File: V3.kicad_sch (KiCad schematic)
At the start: 33 parts, among them J5 MicroMatch, J6 MicroMatch, U1 TL072, U2 TL072, U3 TL072

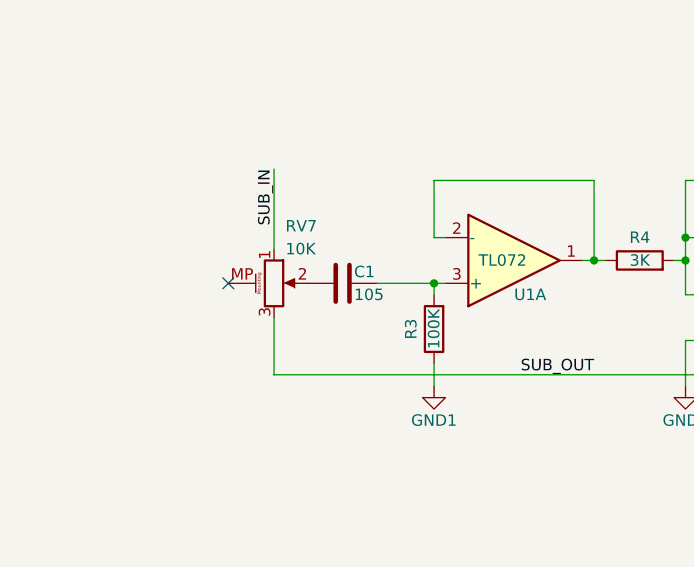
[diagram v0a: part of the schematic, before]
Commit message: Oops, all of the single gang pots were backwards - fixed.
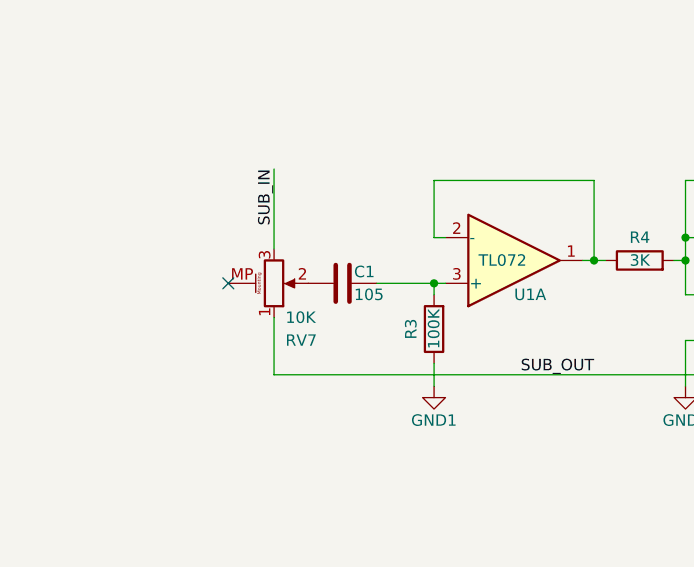
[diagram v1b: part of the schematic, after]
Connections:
- net SUB_IN: now also RV7.3; no longer RV7.1
- net SUB_OUT: now also RV7.1; no longer RV7.3
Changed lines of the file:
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@@
 		(lib_id "Device:R_Potentiometer_MountingPin")
 		(at 63.5 101.6 0)
+		(mirror x)
 		(unit 1)
 		(exclude_from_sim no)
@@
 		(dnp no)
 		(property "Reference" "RV7"
-			(at 64.77 95.25 0)
+			(at 64.77 107.95 0)
 			(effects
 				(font
@@
 		)
 		(property "Value" "10K"
-			(at 64.77 97.79 0)
+			(at 64.77 105.41 0)
 			(effects
 				(font

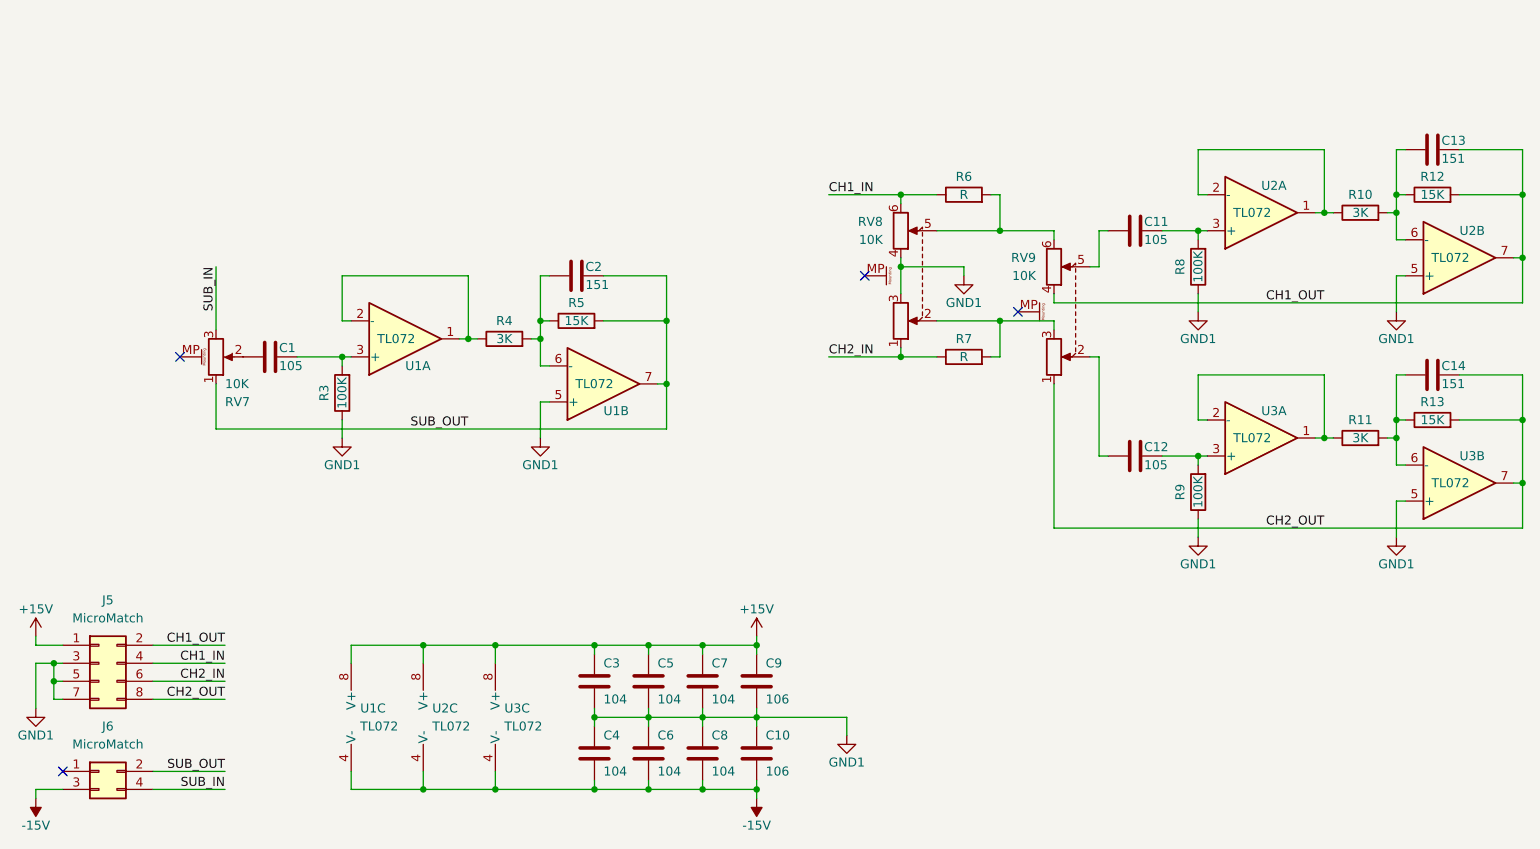
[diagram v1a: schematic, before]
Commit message: Active control topology changed to a single op-amp version.
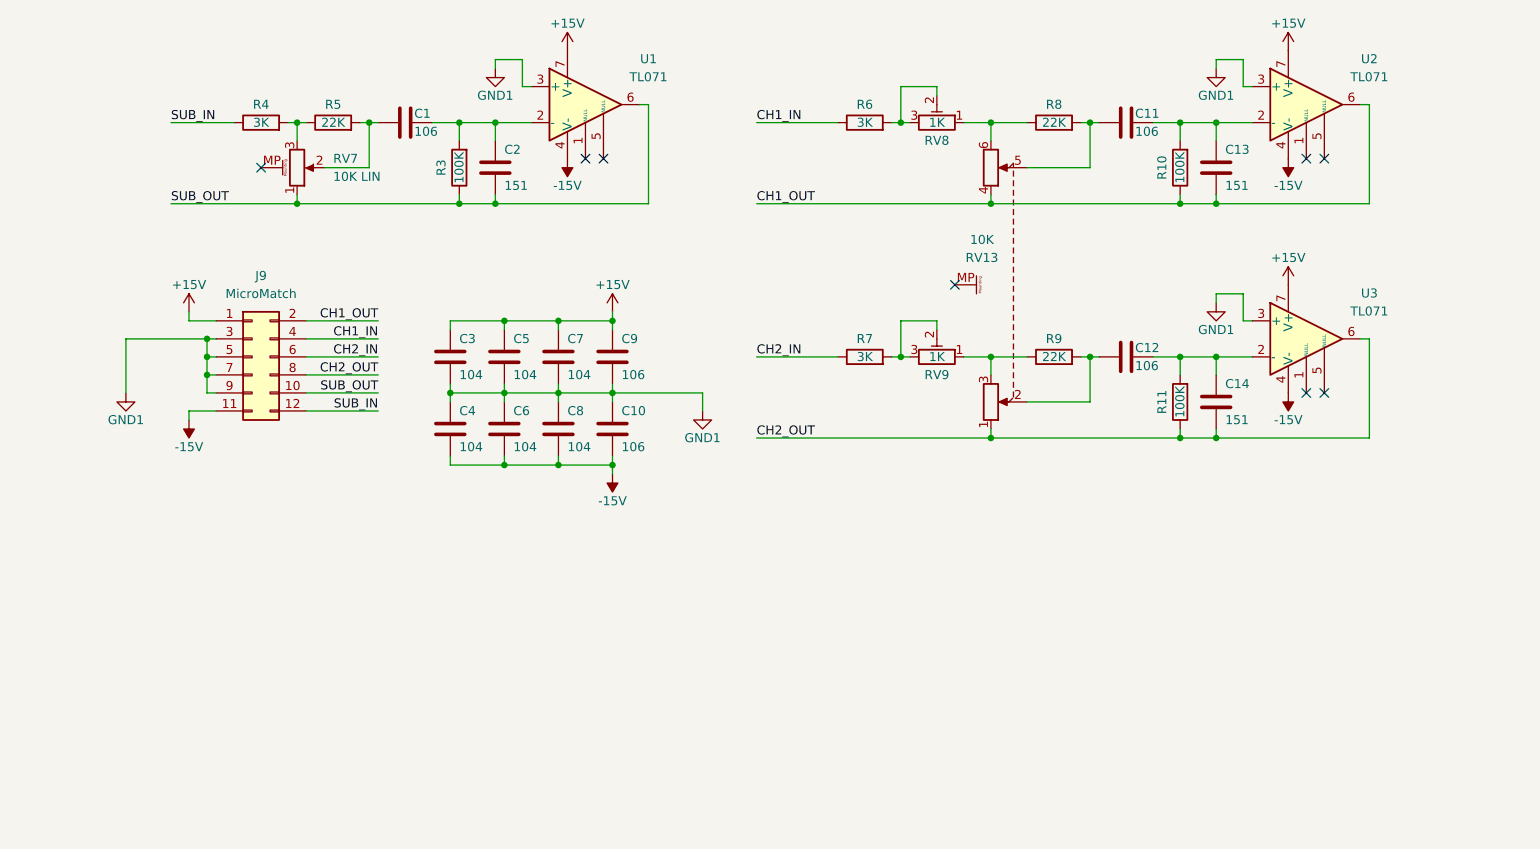
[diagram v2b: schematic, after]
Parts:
- removed J5: MicroMatch, Connector_TE-Connectivity:TE_Micro-MaTch_215079-8_2x04_P1.27mm_Vertical, symbol Connector_Generic:Conn_02x04_Odd_Even
- removed J6: MicroMatch, Connector_TE-Connectivity:TE_Micro-MaTch_215079-4_2x02_P1.27mm_Vertical, symbol Connector_Generic:Conn_02x02_Odd_Even
- removed R12, R13: 15K, Resistor_SMD:R_0805_2012Metric, symbol Device:R
- removed RV8, RV9: 10K, Potentiometer_THT:Potentiometer_Alps_RK09L_Double_Vertical, symbol Device:R_Potentiometer_Dual_MountingPin
- removed U1, U2, U3: TL072, Package_SO:SOIC-8_3.9x4.9mm_P1.27mm, symbol Amplifier_Operational:TL072
- added J9: MicroMatch, Connector_TE-Connectivity:TE_Micro-MaTch_1-215079-2_2x06_P1.27mm_Vertical, symbol Connector_Generic:Conn_02x06_Odd_Even
- added RV13: 10K, Potentiometer_THT:Potentiometer_Alps_RK09L_Double_Vertical, symbol HR_parts:R_Potentiometer_Dual_MountingPin
- added RV8, RV9: 1K, HR_parts:Potentiometer_Bourns_3362P_Vertical, symbol Device:R_Potentiometer_Trim
- added U1, U2, U3: TL071, Package_SO:SOIC-8_3.9x4.9mm_P1.27mm, symbol Amplifier_Operational:TL071
- C1, C11, C12: value 105 -> 106
- R10, R11: value 3K -> 100K
- R5: value 15K -> 22K
- R6, R7: value R -> 3K
- R8, R9: value 100K -> 22K
- RV7: value 10K -> 10K LIN
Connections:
- net +15V: now also J9.1 (Pin_1), U1.7 (V+), U2.7 (V+), U3.7 (V+)
- net -15V: now also J9.11 (Pin_11), U1.4 (V-), U2.4 (V-), U3.4 (V-)
- net CH1_IN: now also J9.4 (Pin_4)
- net CH1_OUT: now also R10.1, J9.2 (Pin_2), RV13.4, U2.6
- net CH2_IN: now also J9.6 (Pin_6)
- net CH2_OUT: now also R11.1, J9.8 (Pin_8), RV13.1, U3.6
- net GND1: now also J9.3 (Pin_3), J9.5 (Pin_5), J9.7 (Pin_7), J9.9 (Pin_9), U1.3 (+), U2.3 (+), U3.3 (+); no longer R3.1, R8.1, R9.1
- net SUB_IN: now also R4.1, J9.12 (Pin_12); no longer RV7.3
- net SUB_OUT: now also R3.1, J9.10 (Pin_10), U1.6; no longer R5.2
- net at R9.2: now also C12.1, RV13.2; no longer C12.2
- net at R7.2: now also RV9.2, RV9.3
- net at C13.1, R10.2: now also C11.2, U2.2 (-)
- net at C11.1: now also R8.2, RV13.5
- net at R6.2: now also RV8.2, RV8.3
- net at C1.2, R3.2: now also C2.1, U1.2 (-)
- net at C14.1, R11.2: now also C12.2, U3.2 (-)
- net at R4.2, R5.1: now also RV7.3; no longer C2.1
- net at C1.1, RV7.2: now also R5.2
- new net: R9.1, RV13.3, RV9.1
- new net: R8.1, RV13.6, RV8.1
- no-connect marks 4 -> 8
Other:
- moved on the sheet: C1, C10, C3, C4, C5, C6, C7, C8, C9, R3, R4, R5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
